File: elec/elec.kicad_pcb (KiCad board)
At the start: 2 copper layers, 6 parts, among them Q1 AO3401A, U1 HUSB238A-xxxxx-QN16R, U2 SY8303AIC, U3 STM32G030K8T6, U4 TPS55289RYQR, U6 IS31FL3731-QF

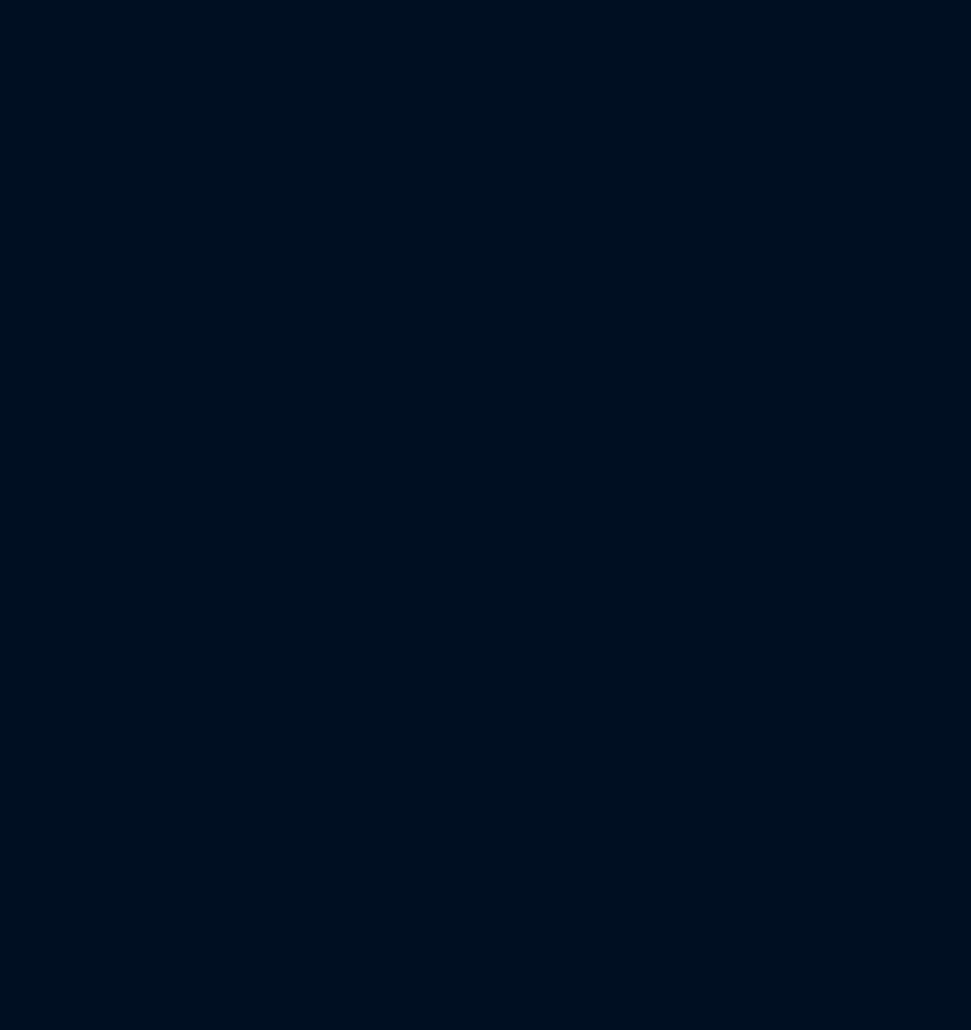
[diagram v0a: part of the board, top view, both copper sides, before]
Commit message: Populate LCSC Params, Assign Footprints, Update STM32CubeMX
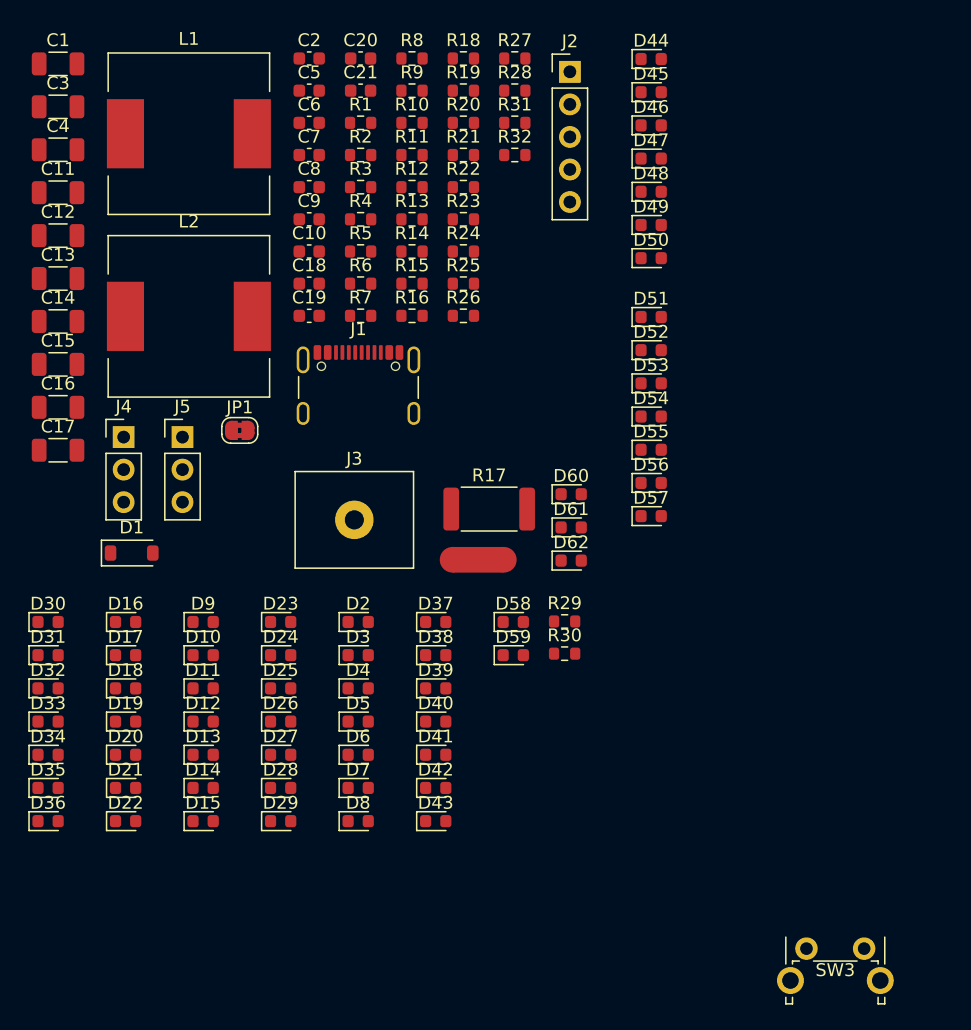
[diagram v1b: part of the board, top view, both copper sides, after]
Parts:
- added C1: 4u7, Capacitor_SMD:C_1206_3216Metric, F.Cu at (49.8, 60.2)
- added C10: 0.1uF, Capacitor_SMD:C_0603_1608Metric, F.Cu at (69.4, 74.8)
- added C11: 22uF, Capacitor_SMD:C_1206_3216Metric, F.Cu at (49.8, 70.2)
- added C12: 10uF, Capacitor_SMD:C_1206_3216Metric, F.Cu at (49.8, 73.6)
- added C13: 22uF, Capacitor_SMD:C_1206_3216Metric, F.Cu at (49.8, 76.9)
- added C14: 22uF, Capacitor_SMD:C_1206_3216Metric, F.Cu at (49.8, 80.3)
- added C15: 22uF, Capacitor_SMD:C_1206_3216Metric, F.Cu at (49.8, 83.6)
- added C16: 22uF, Capacitor_SMD:C_1206_3216Metric, F.Cu at (49.8, 87.0)
- added C17: 22uF, Capacitor_SMD:C_1206_3216Metric, F.Cu at (49.8, 90.3)
- added C18: 100pF, Capacitor_SMD:C_0603_1608Metric, F.Cu at (69.4, 77.3)
- added C19: 1uF, Capacitor_SMD:C_0603_1608Metric, F.Cu at (69.4, 79.8)
- added C2: 0.1uF, Capacitor_SMD:C_0603_1608Metric, F.Cu at (69.4, 59.8)
- added C20: 0.1uF, Capacitor_SMD:C_0603_1608Metric, F.Cu at (73.4, 59.8)
- added C21: 0.1uF, Capacitor_SMD:C_0603_1608Metric, F.Cu at (73.4, 62.3)
- added C3: 4u7, Capacitor_SMD:C_1206_3216Metric, F.Cu at (49.8, 63.5)
- added C4: 4u7, Capacitor_SMD:C_1206_3216Metric, F.Cu at (49.8, 66.9)
- added C5: 10pF, Capacitor_SMD:C_0603_1608Metric, F.Cu at (69.4, 62.3)
- added C6: 0.1uF, Capacitor_SMD:C_0603_1608Metric, F.Cu at (69.4, 64.8)
- added C7: 0.1uF, Capacitor_SMD:C_0603_1608Metric, F.Cu at (69.4, 67.3)
- added C8: 0.1uF, Capacitor_SMD:C_0603_1608Metric, F.Cu at (69.4, 69.8)
- added C9: 0.1uF, Capacitor_SMD:C_0603_1608Metric, F.Cu at (69.4, 72.3)
- added D1: D_Zener, Diode_SMD:D_SOD-123, F.Cu at (55.6, 98.3)
- added D10: LED, LED_SMD:LED_0603_1608Metric, F.Cu at (61.1, 106.3)
- added D11: LED, LED_SMD:LED_0603_1608Metric, F.Cu at (61.1, 108.9)
- added D12: LED, LED_SMD:LED_0603_1608Metric, F.Cu at (61.1, 111.5)
- added D13: LED, LED_SMD:LED_0603_1608Metric, F.Cu at (61.1, 114.1)
- added D14: LED, LED_SMD:LED_0603_1608Metric, F.Cu at (61.1, 116.7)
- added D15: LED, LED_SMD:LED_0603_1608Metric, F.Cu at (61.1, 119.3)
- added D16: LED, LED_SMD:LED_0603_1608Metric, F.Cu at (55.1, 103.7)
- added D17: LED, LED_SMD:LED_0603_1608Metric, F.Cu at (55.1, 106.3)
- added D18: LED, LED_SMD:LED_0603_1608Metric, F.Cu at (55.1, 108.9)
- added D19: LED, LED_SMD:LED_0603_1608Metric, F.Cu at (55.1, 111.5)
- added D2: LED, LED_SMD:LED_0603_1608Metric, F.Cu at (73.2, 103.7)
- added D20: LED, LED_SMD:LED_0603_1608Metric, F.Cu at (55.1, 114.1)
- added D21: LED, LED_SMD:LED_0603_1608Metric, F.Cu at (55.1, 116.7)
- added D22: LED, LED_SMD:LED_0603_1608Metric, F.Cu at (55.1, 119.3)
- added D23: LED, LED_SMD:LED_0603_1608Metric, F.Cu at (67.2, 103.7)
- added D24: LED, LED_SMD:LED_0603_1608Metric, F.Cu at (67.2, 106.3)
- added D25: LED, LED_SMD:LED_0603_1608Metric, F.Cu at (67.2, 108.9)
- added D26: LED, LED_SMD:LED_0603_1608Metric, F.Cu at (67.2, 111.5)
- added D27: LED, LED_SMD:LED_0603_1608Metric, F.Cu at (67.2, 114.1)
- added D28: LED, LED_SMD:LED_0603_1608Metric, F.Cu at (67.2, 116.7)
- added D29: LED, LED_SMD:LED_0603_1608Metric, F.Cu at (67.2, 119.3)
- added D3: LED, LED_SMD:LED_0603_1608Metric, F.Cu at (73.2, 106.3)
- added D30: LED, LED_SMD:LED_0603_1608Metric, F.Cu at (49.0, 103.7)
- added D31: LED, LED_SMD:LED_0603_1608Metric, F.Cu at (49.0, 106.3)
- added D32: LED, LED_SMD:LED_0603_1608Metric, F.Cu at (49.0, 108.9)
- added D33: LED, LED_SMD:LED_0603_1608Metric, F.Cu at (49.0, 111.5)
- added D34: LED, LED_SMD:LED_0603_1608Metric, F.Cu at (49.0, 114.1)
- added D35: LED, LED_SMD:LED_0603_1608Metric, F.Cu at (49.0, 116.7)
- added D36: LED, LED_SMD:LED_0603_1608Metric, F.Cu at (49.0, 119.3)
- added D37: LED, LED_SMD:LED_0603_1608Metric, F.Cu at (79.3, 103.7)
- added D38: LED, LED_SMD:LED_0603_1608Metric, F.Cu at (79.3, 106.3)
- added D39: LED, LED_SMD:LED_0603_1608Metric, F.Cu at (79.3, 108.9)
- added D4: LED, LED_SMD:LED_0603_1608Metric, F.Cu at (73.2, 108.9)
- added D40: LED, LED_SMD:LED_0603_1608Metric, F.Cu at (79.3, 111.5)
- added D41: LED, LED_SMD:LED_0603_1608Metric, F.Cu at (79.3, 114.1)
- added D42: LED, LED_SMD:LED_0603_1608Metric, F.Cu at (79.3, 116.7)
- added D43: LED, LED_SMD:LED_0603_1608Metric, F.Cu at (79.3, 119.3)
- added D44: LED, LED_SMD:LED_0603_1608Metric, F.Cu at (96.1, 59.8)
- added D45: LED, LED_SMD:LED_0603_1608Metric, F.Cu at (96.1, 62.4)
- added D46: LED, LED_SMD:LED_0603_1608Metric, F.Cu at (96.1, 65.0)
- added D47: LED, LED_SMD:LED_0603_1608Metric, F.Cu at (96.1, 67.6)
- added D48: LED, LED_SMD:LED_0603_1608Metric, F.Cu at (96.1, 70.2)
- added D49: LED, LED_SMD:LED_0603_1608Metric, F.Cu at (96.1, 72.7)
- added D5: LED, LED_SMD:LED_0603_1608Metric, F.Cu at (73.2, 111.5)
- added D50: LED, LED_SMD:LED_0603_1608Metric, F.Cu at (96.1, 75.3)
- added D51: LED, LED_SMD:LED_0603_1608Metric, F.Cu at (96.1, 79.9)
- added D52: LED, LED_SMD:LED_0603_1608Metric, F.Cu at (96.1, 82.5)
- added D53: LED, LED_SMD:LED_0603_1608Metric, F.Cu at (96.1, 85.1)
- added D54: LED, LED_SMD:LED_0603_1608Metric, F.Cu at (96.1, 87.7)
- added D55: LED, LED_SMD:LED_0603_1608Metric, F.Cu at (96.1, 90.3)
- added D56: LED, LED_SMD:LED_0603_1608Metric, F.Cu at (96.1, 92.9)
- added D57: LED, LED_SMD:LED_0603_1608Metric, F.Cu at (96.1, 95.5)
- added D58: LED, LED_SMD:LED_0603_1608Metric, F.Cu at (85.3, 103.7)
- added D59: LED, LED_SMD:LED_0603_1608Metric, F.Cu at (85.3, 106.3)
- added D6: LED, LED_SMD:LED_0603_1608Metric, F.Cu at (73.2, 114.1)
- added D60: LED, LED_SMD:LED_0603_1608Metric, F.Cu at (89.9, 93.8)
- added D61: LED, LED_SMD:LED_0603_1608Metric, F.Cu at (89.9, 96.3)
- added D62: LED, LED_SMD:LED_0603_1608Metric, F.Cu at (89.9, 98.9)
- added D7: LED, LED_SMD:LED_0603_1608Metric, F.Cu at (73.2, 116.7)
- added D8: LED, LED_SMD:LED_0603_1608Metric, F.Cu at (73.2, 119.3)
- added D9: LED, LED_SMD:LED_0603_1608Metric, F.Cu at (61.1, 103.7)
- added J1: USB_C_Receptacle, Connector_USB:USB_C_Receptacle_GCT_USB4105-xx-A_16P_TopMnt_Horizontal, F.Cu at (73.3, 86.4)
- added J2: Conn_01x05, Connector_PinHeader_2.54mm:PinHeader_1x05_P2.54mm_Vertical, F.Cu at (89.8, 60.8)
- added J3: Screw_Terminal_01x02, TerminalBlock_MetzConnect:TerminalBlock_MetzConnect_360271_1x01_Horizontal_ScrewM3.0_Boxed, F.Cu at (72.9, 95.8)
- added J4: Conn_01x03, Connector_PinHeader_2.54mm:PinHeader_1x03_P2.54mm_Vertical, F.Cu at (54.9, 89.3)
- added J5: Conn_01x03, Connector_PinHeader_2.54mm:PinHeader_1x03_P2.54mm_Vertical, F.Cu at (59.5, 89.3)
- added JP1: SolderJumper_2_Bridged, Jumper:SolderJumper-2_P1.3mm_Bridged2Bar_RoundedPad1.0x1.5mm, F.Cu at (64.0, 88.8)
- added L1: 47uH, Inductor_SMD:L_12x12mm_H8mm, F.Cu at (60.0, 65.6)
- added L2: 4.7uH, Inductor_SMD:L_12x12mm_H8mm, F.Cu at (60.0, 79.9)
- added NT1: NetTie_2, NetTie:NetTie-2_SMD_Pad2.0mm, F.Cu at (82.6, 98.9)
- added R1: 20k, Resistor_SMD:R_0603_1608Metric, F.Cu at (73.4, 64.8)
- added R10: 470R, Resistor_SMD:R_0603_1608Metric, F.Cu at (77.4, 64.8)
- added R11: 20k, Resistor_SMD:R_0603_1608Metric, F.Cu at (77.4, 67.3)
- added R12: 2k2, Resistor_SMD:R_0603_1608Metric, F.Cu at (77.4, 69.8)
- added R13: 2k2, Resistor_SMD:R_0603_1608Metric, F.Cu at (77.4, 72.3)
- added R14: 20k, Resistor_SMD:R_0603_1608Metric, F.Cu at (77.4, 74.8)
- added R15: 100k, Resistor_SMD:R_0603_1608Metric, F.Cu at (77.4, 77.3)
- added R16: 100k, Resistor_SMD:R_0603_1608Metric, F.Cu at (77.4, 79.8)
- added R17: 15m, Resistor_SMD:R_2512_6332Metric, F.Cu at (83.5, 94.9)
- added R18: 20k, Resistor_SMD:R_0603_1608Metric, F.Cu at (81.5, 59.8)
- added R19: 20k, Resistor_SMD:R_0603_1608Metric, F.Cu at (81.5, 62.3)
- added R2: 20k, Resistor_SMD:R_0603_1608Metric, F.Cu at (73.4, 67.3)
- added R20: 147k, Resistor_SMD:R_0603_1608Metric, F.Cu at (81.5, 64.8)
- added R21: 20k, Resistor_SMD:R_0603_1608Metric, F.Cu at (81.5, 67.3)
- added R22: 20k, Resistor_SMD:R_0603_1608Metric, F.Cu at (81.5, 69.8)
- added R23: 20k, Resistor_SMD:R_0603_1608Metric, F.Cu at (81.5, 72.3)
- added R24: 20k, Resistor_SMD:R_0603_1608Metric, F.Cu at (81.5, 74.8)
- added R25: 20k, Resistor_SMD:R_0603_1608Metric, F.Cu at (81.5, 77.3)
- added R26: 1k, Resistor_SMD:R_0603_1608Metric, F.Cu at (81.5, 79.8)
- added R27: 1k, Resistor_SMD:R_0603_1608Metric, F.Cu at (85.5, 59.8)
- added R28: 1k, Resistor_SMD:R_0603_1608Metric, F.Cu at (85.5, 62.3)
- added R29: 20k, Resistor_SMD:R_0603_1608Metric, F.Cu at (89.4, 103.7)
- added R3: 20k, Resistor_SMD:R_0603_1608Metric, F.Cu at (73.4, 69.8)
- added R30: 20k, Resistor_SMD:R_0603_1608Metric, F.Cu at (89.4, 106.2)
- added R31: 10k, Resistor_SMD:R_0603_1608Metric, F.Cu at (85.5, 64.8)
- added R32: 1k, Resistor_SMD:R_0603_1608Metric, F.Cu at (85.5, 67.3)
- added R4: 20k, Resistor_SMD:R_0603_1608Metric, F.Cu at (73.4, 72.3)
- added R5: 20k, Resistor_SMD:R_0603_1608Metric, F.Cu at (73.4, 74.8)
- added R6: 2k2, Resistor_SMD:R_0603_1608Metric, F.Cu at (73.4, 77.3)
- added R7: 900k, Resistor_SMD:R_0603_1608Metric, F.Cu at (73.4, 79.8)
- added R8: 900k, Resistor_SMD:R_0603_1608Metric, F.Cu at (77.4, 59.8)
- added R9: 100k, Resistor_SMD:R_0603_1608Metric, F.Cu at (77.4, 62.3)
- added SW3: SW_Push, Button_Switch_THT:SW_Tactile_SPST_Angled_PTS645Vx58-2LFS, F.Cu at (108.2, 129.2)
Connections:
- U3 pad 11: unconnected-(U3-PA4-Pad11) -> /TEMP_ADC
- U3 pad 12: unconnected-(U3-PA5-Pad12) -> /TEMP_INDICATOR
- U3 pad 13: unconnected-(U3-PA6-Pad13) -> /USB-C_EN
- U3 pad 14: unconnected-(U3-PA7-Pad14) -> /USB-C_Fault_IN
- U3 pad 15: /BUTTON_CURR_+ -> /USB-C_Fault
- U3 pad 16: /BUTTON_CURR_- -> /USB-C_INT
- U3 pad 17: /BUTTON_VOLT_+ -> /PB2
- U3 pad 18: unconnected-(U3-PA8-Pad18) -> /BUTTON_OUTPUT
- U3 pad 19: unconnected-(U3-NC/PA9-Pad19) -> /BUTTON_VOLT_-
- U3 pad 20: unconnected-(U3-PC6-Pad20) -> /BUTTON_VOLT_+
- U3 pad 21: unconnected-(U3-NC/PA10-Pad21) -> /BUTTON_CURR_-
- U3 pad 22: unconnected-(U3-PA9/PA11-Pad22) -> /BUTTON_CURR_+
- U3 pad 23: unconnected-(U3-PA10/PA12-Pad23) -> /BUCK-BOOST_Fault
- U3 pad 26: unconnected-(U3-PA15-Pad26) -> /BUCK-BOOST_EN
- U3 pad 28: unconnected-(U3-PB4-Pad28) -> /VOUT_FAULT_INDICATOR
- U3 pad 29: unconnected-(U3-PB5-Pad29) -> /USB_FAULT_INDICATOR
- U4 pad 16: unconnected-(U4-CDC-Pad16) -> /BUCK-BOOST_Current
- U4 pad 7: VBUS -> Net-(JP1-A)

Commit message: Start PCB Layout Draft
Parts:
- added SW2: SW_Push, Button_Switch_THT:SW_Tactile_SPST_Angled_PTS645Vx58-2LFS, F.Cu at (226.3, 89.6)
- added SW4: SW_Push, Button_Switch_THT:SW_Tactile_SPST_Angled_PTS645Vx58-2LFS, F.Cu at (236.9, 89.6)
- added SW5: SW_Push, Button_Switch_THT:SW_Tactile_SPST_Angled_PTS645Vx58-2LFS, F.Cu at (247.5, 89.6)
- added SW6: SW_Push, Button_Switch_THT:SW_Tactile_SPST_Angled_PTS645Vx58-2LFS, F.Cu at (258.1, 89.6)
- added SW7: SW_Push, Button_Switch_THT:SW_Tactile_SPST_Angled_PTS645Vx58-2LFS, F.Cu at (268.7, 89.6)
- added TH1: Thermistor_NTC, Resistor_SMD:R_0603_1608Metric, F.Cu at (225.2, 95.8)
- C10, C11, C13, C14, C15, C16, C17, C18, C19, C9, JP1, R20: moved to B.Cu
- L1: footprint Inductor_SMD:L_12x12mm_H8mm -> Inductor_SMD:L_APV_ANR5040
- moved C20 117.2 mm to (189.7, 74.4)
- moved C21 117.2 mm to (189.7, 76.9)
- moved D16 117.2 mm to (171.3, 118.4)
- moved D17 117.2 mm to (171.3, 121.0)
- moved D18 117.2 mm to (171.3, 123.6)
- moved D19 117.2 mm to (171.3, 126.2)
- moved D2 117.2 mm to (189.5, 118.4)
- moved D20 117.2 mm to (171.3, 128.8)
- moved D21 117.2 mm to (171.3, 131.3)
- moved D22 117.2 mm to (171.3, 133.9)
- moved D23 117.2 mm to (183.4, 118.4)
- moved D24 117.2 mm to (183.4, 121.0)
- moved D25 117.2 mm to (183.4, 123.6)
- moved D26 117.2 mm to (183.4, 126.2)
- moved D27 117.2 mm to (183.4, 128.8)
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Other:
- board outline added: 44.2 x 46 mm

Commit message: Layout of everything except display
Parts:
- added H1: MountingHole_Pad, MountingHole:MountingHole_2.2mm_M2_Pad_Via, F.Cu at (150.5, 136.5)
- added H2: MountingHole, MountingHole:MountingHole_2.2mm_M2_Pad_Via, F.Cu at (150.5, 83.5)
- added H3: MountingHole, MountingHole:MountingHole_2.2mm_M2_Pad_Via, F.Cu at (97.5, 83.5)
- added H4: MountingHole, MountingHole:MountingHole_2.2mm_M2_Pad_Via, F.Cu at (97.5, 136.5)
- added R33: 0R, Resistor_SMD:R_0603_1608Metric, F.Cu at (146.8, 136.5)
- J3: footprint TerminalBlock_MetzConnect:TerminalBlock_MetzConnect_360271_1x01_Horizontal_ScrewM3.0_Boxed -> TerminalBlock_CUI:TerminalBlock_CUI_TB007-508-02_1x02_P5.08mm_Horizontal
- R14, R15, R16: moved to B.Cu
- SW2: footprint Button_Switch_THT:SW_Tactile_SPST_Angled_PTS645Vx58-2LFS -> usbc-psu-footprints:SKRKAEE020
- moved U6 242.0 mm to (27.1, 34.9)
- moved D10 203.7 mm to (-7.00, 34.3)
- moved D12 203.7 mm to (-7.00, 39.5)
- moved D13 203.7 mm to (-7.00, 42.1)
- moved D14 203.7 mm to (-7.00, 44.7)
- moved D15 203.7 mm to (-7.00, 47.2)
- moved D16 203.7 mm to (-13.0, 31.7)
- moved D17 203.7 mm to (-13.0, 34.3)
- moved D19 203.7 mm to (-13.0, 39.5)
- moved D2 203.7 mm to (5.10, 31.7)
- moved D20 203.7 mm to (-13.0, 42.1)
- moved D21 203.7 mm to (-13.0, 44.7)
- moved D22 203.7 mm to (-13.0, 47.2)
- moved D23 203.7 mm to (-0.95, 31.7)
- moved D24 203.7 mm to (-0.95, 34.3)
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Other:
- board size 44.2 x 46 mm -> 58 x 58 mm

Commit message: PCB layout
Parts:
- added D63: LED, LED_SMD:LED_0603_1608Metric, F.Cu at (142.7, 83.8)
- added D64: LED, LED_SMD:LED_0603_1608Metric, F.Cu at (142.7, 89.5)
- added D65: LED, LED_SMD:LED_0603_1608Metric, F.Cu at (142.7, 95.2)
- added R34: 1k, Resistor_SMD:R_0603_1608Metric, F.Cu at (142.7, 85.4)
- added R35: 1k, Resistor_SMD:R_0603_1608Metric, F.Cu at (142.7, 91.1)
- added R36: 1k, Resistor_SMD:R_0603_1608Metric, F.Cu at (142.7, 96.8)
- NT1: moved to B.Cu
- moved D16 149.7 mm to (127.2, 84.1)
- moved D19 149.2 mm to (127.2, 90.3)
- moved D18 149.1 mm to (127.2, 87.3)
- moved D22 148.4 mm to (129.4, 88.8), turned to -90 degrees
- moved D21 148.2 mm to (129.4, 85.5), turned to 90 degrees
- moved D17 147.2 mm to (124.9, 85.5), turned to 90 degrees
- moved D20 145.7 mm to (124.9, 88.8), turned to -90 degrees
- moved D23 145.1 mm to (134.4, 84.1)
- moved D26 144.6 mm to (134.4, 90.3)
- moved D25 144.5 mm to (134.4, 87.3)
- moved D44 144.4 mm to (127.2, 92.7)
- moved D29 143.7 mm to (136.7, 88.8), turned to -90 degrees
- moved D28 143.5 mm to (136.7, 85.5), turned to 90 degrees
- moved D47 143.3 mm to (127.2, 99.0)
- moved D46 143.1 mm to (127.2, 96.0)
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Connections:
- U3 pad 7: unconnected-(U3-PA0-Pad7) -> /CV_INDICATOR
- U3 pad 8: unconnected-(U3-PA1-Pad8) -> /CC_INDICATOR
- U3 pad 9: unconnected-(U3-PA2-Pad9) -> /OCP_INDICATOR
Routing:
- net /display/SEG_G: vias 0 -> 8
- net /display/SEG_F: vias 0 -> 8
- net /display/SEG_E: vias 0 -> 8
- net /display/SEG_D: vias 0 -> 8
- net /display/SEG_C: vias 0 -> 8
- net /display/SEG_B: vias 0 -> 8
- net /display/SEG_A: vias 0 -> 8
- added copper zone on F.Cu, net /display/DIG_0
- added copper zone on F.Cu, net /display/DIG_1
- added copper zone on F.Cu, net /display/DIG_2
- added copper zone on F.Cu, net /display/DIG_3
- added copper zone on F.Cu, net /display/DIG_4
- added copper zone on F.Cu, net /display/DIG_5
- added copper zone on F.Cu, net /display/DIG_6
- added copper zone on F.Cu, net /display/DIG_7
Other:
- board text added: "'26-6-19"
- board text added: "A"
- board text added: "CC"
- board text added: "CV"
- board text added: "I +"
- board text added: "I -"
- board text added: "I2C"
- board text added: "OCP"
- board text added: "OUT"
- board text added: "OUT +"
- board text added: "OUT -"
- board text added: "ST-LINK"
- board text added: "TEMP"
- board text added: "UART"
- board text added: "USB FAULT"
- board text added: "USB-C PSU"
- board text added: "V"
- board text added: "V +"
- board text added: "V -"
- board text added: "V FAULT"
- board text added: "rev 1"

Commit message: Completed Routing
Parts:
- NT1: moved to F.Cu
- Q1: value AO3401A -> AO4419; footprint Package_TO_SOT_SMD:SOT-23 -> Package_SO:SOIC-8-1EP_3.9x4.9mm_P1.27mm_EP2.29x3mm_ThermalVias
- moved C20 12.0 mm to (135.9, 113.3), turned to -90 degrees
- moved R31 9.50 mm to (134.2, 113.3), turned to 90 degrees
- moved TH1 7.03 mm to (132.4, 113.3), turned to -90 degrees
- moved R7 5.54 mm to (110.4, 104.5), turned to 90 degrees
- moved R8 4.06 mm to (110.4, 107.8)
- moved NT1 3.31 mm to (143.4, 114.8)
- moved C9 3.03 mm to (139.2, 125.1), turned to 0 degrees
- moved C10 2.93 mm to (139.0, 120.2), turned to 0 degrees
- moved Q1 2.51 mm to (107.2, 115.6), turned to 180 degrees
- moved U6 2.39 mm to (115.5, 104.7)
- moved R17 2.36 mm to (147.7, 123.3)
- moved C11 2.30 mm to (142.2, 127.1)
- moved C12 2.30 mm to (143.5, 117.0)
- moved C13 2.30 mm to (144.7, 127.1)
- moved C14 2.30 mm to (139.2, 116.9)
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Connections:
- D10 pad 1: /display/DIG_1 -> /display/DIG_5
- D11 pad 1: /display/DIG_1 -> /display/DIG_5
- D12 pad 1: /display/DIG_1 -> /display/DIG_5
- D13 pad 1: /display/DIG_1 -> /display/DIG_5
- D14 pad 1: /display/DIG_1 -> /display/DIG_5
- D15 pad 1: /display/DIG_1 -> /display/DIG_5
- D16 pad 1: /display/DIG_2 -> /display/DIG_3
- D17 pad 1: /display/DIG_2 -> /display/DIG_3
- D18 pad 1: /display/DIG_2 -> /display/DIG_3
- D19 pad 1: /display/DIG_2 -> /display/DIG_3
- D2 pad 1: /display/DIG_0 -> /display/DIG_7
- D20 pad 1: /display/DIG_2 -> /display/DIG_3
- D21 pad 1: /display/DIG_2 -> /display/DIG_3
- D22 pad 1: /display/DIG_2 -> /display/DIG_3
- D23 pad 1: /display/DIG_3 -> /display/DIG_1
- D24 pad 1: /display/DIG_3 -> /display/DIG_1
- D25 pad 1: /display/DIG_3 -> /display/DIG_1
- D26 pad 1: /display/DIG_3 -> /display/DIG_1
- D27 pad 1: /display/DIG_3 -> /display/DIG_1
- D28 pad 1: /display/DIG_3 -> /display/DIG_1
- D29 pad 1: /display/DIG_3 -> /display/DIG_1
- D3 pad 1: /display/DIG_0 -> /display/DIG_7
- D30 pad 1: /display/DIG_4 -> /display/DIG_6
- D31 pad 1: /display/DIG_4 -> /display/DIG_6
- D32 pad 1: /display/DIG_4 -> /display/DIG_6
- D33 pad 1: /display/DIG_4 -> /display/DIG_6
- D34 pad 1: /display/DIG_4 -> /display/DIG_6
- D35 pad 1: /display/DIG_4 -> /display/DIG_6
- D36 pad 1: /display/DIG_4 -> /display/DIG_6
- D37 pad 1: /display/DIG_5 -> /display/DIG_4
- D38 pad 1: /display/DIG_5 -> /display/DIG_4
- D39 pad 1: /display/DIG_5 -> /display/DIG_4
- D4 pad 1: /display/DIG_0 -> /display/DIG_7
- D40 pad 1: /display/DIG_5 -> /display/DIG_4
- D41 pad 1: /display/DIG_5 -> /display/DIG_4
- D42 pad 1: /display/DIG_5 -> /display/DIG_4
- D43 pad 1: /display/DIG_5 -> /display/DIG_4
- D44 pad 1: /display/DIG_6 -> /display/DIG_2
- D45 pad 1: /display/DIG_6 -> /display/DIG_2
- D46 pad 1: /display/DIG_6 -> /display/DIG_2
- D47 pad 1: /display/DIG_6 -> /display/DIG_2
- D48 pad 1: /display/DIG_6 -> /display/DIG_2
- D49 pad 1: /display/DIG_6 -> /display/DIG_2
- D5 pad 1: /display/DIG_0 -> /display/DIG_7
- D50 pad 1: /display/DIG_6 -> /display/DIG_2
- D51 pad 1: /display/DIG_7 -> /display/DIG_0
- D52 pad 1: /display/DIG_7 -> /display/DIG_0
- D53 pad 1: /display/DIG_7 -> /display/DIG_0
- D54 pad 1: /display/DIG_7 -> /display/DIG_0
- D55 pad 1: /display/DIG_7 -> /display/DIG_0
- D56 pad 1: /display/DIG_7 -> /display/DIG_0
- D57 pad 1: /display/DIG_7 -> /display/DIG_0
- D59 pad 1: /display/DIG_7 -> /display/DIG_2
- D6 pad 1: /display/DIG_0 -> /display/DIG_7
- D7 pad 1: /display/DIG_0 -> /display/DIG_7
- D8 pad 1: /display/DIG_0 -> /display/DIG_7
- D9 pad 1: /display/DIG_1 -> /display/DIG_5
- R34 pad 1: /display/CV_INDICATOR -> /CV_INDICATOR
- R35 pad 1: /display/CC_INDICATOR -> /CC_INDICATOR
- R36 pad 1: /display/OCP_INDICATOR -> /OCP_INDICATOR
- U3 pad 12: /TEMP_INDICATOR -> /USB_FAULT_INDICATOR
- U3 pad 18: /BUTTON_OUTPUT -> /BUTTON_VOLT_+
- U3 pad 20: /BUTTON_VOLT_+ -> /BUTTON_CURR_+
- U3 pad 22: /BUTTON_CURR_+ -> /BUTTON_OUTPUT
- U3 pad 27: /BUTTON_VOLT_- -> unconnected-(U3-PB3-Pad27)
- U3 pad 29: /USB_FAULT_INDICATOR -> /TEMP_INDICATOR
- U3 pad 7: /CV_INDICATOR -> /OCP_INDICATOR
- U3 pad 9: /OCP_INDICATOR -> /CV_INDICATOR
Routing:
- net +3V3: track 0.00 -> 215.6 mm, vias 0 -> 15
- net /SDA: track 0.00 -> 119.6 mm, vias 0 -> 6
- net /SCL: track 0.00 -> 117.2 mm, vias 0 -> 6
- net /display/SEG_B: track 0.00 -> 108.4 mm, vias 8 -> 10
- net /display/SEG_A: track 0.00 -> 90.0 mm, vias 8 -> 10
- net /display/SEG_E: track 0.00 -> 81.9 mm
- net /display/SEG_C: track 0.00 -> 81.9 mm
- net /display/SEG_F: track 0.00 -> 75.5 mm, vias 8 -> 10
- net /display/SEG_D: track 0.00 -> 73.4 mm
- net /display/SEG_G: track 0.00 -> 67.8 mm
- net /BUTTON_OUTPUT: track 0.00 -> 52.4 mm
- net /BUCK-BOOST_Current: track 0.00 -> 50.5 mm, vias 0 -> 2
- net /NRST: track 0.00 -> 49.4 mm, vias 0 -> 1
- net /USB_FAULT_INDICATOR: track 0.00 -> 45.8 mm, vias 0 -> 2
- net /SWCLK: track 0.00 -> 44.0 mm, vias 0 -> 1
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- added copper zone on F.Cu, net +3V3
- added copper zone on F.Cu, net AGND
- added copper zone on F.Cu, net GNDREF
- added copper zone on In1.Cu, net GNDREF
- added copper zone on In2.Cu, net GNDREF
- added copper zone on B.Cu, net Net-(JP1-A)
- added copper zone on F.Cu, net Net-(JP1-A)
- added copper zone on F.Cu, net Net-(U2-LX)
- added copper zone on B.Cu, net Net-(U4-ISP)
- added copper zone on F.Cu, net Net-(U4-ISP)
- added copper zone on F.Cu, net Net-(U4-SW1)
- added copper zone on F.Cu, net Net-(U4-SW2)
- added copper zone on B.Cu, net VBUS
- added copper zone on F.Cu, net VBUS
- added copper zone on F.Cu, net VBUS_RAW
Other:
- copper layers 2 -> 4
- board text added: "'26-6-22"
- board text added: "PORTABLE"
- board text added: "PSU"
- board text added: "Stackup: SIG + PWR / GND / GND / PWR + SIG"
- board text added: "USB-C PD"
- board text added: "design of chen-xuan, 2026"
- board text added: "github.com/Ng-Chen-Xuan/USB-C-Portable-PSU"
- board text removed: "'26-6-19"
